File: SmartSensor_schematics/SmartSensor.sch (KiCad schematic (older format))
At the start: 48 parts, among them IC1 DS1337+, J1 Conn_01x01_Female, J2 Conn_01x01_Female, J3 Conn_02x04_Odd_Even, J4 FTDI cable connector, J5 USB_B_Micro, J8 6 PIN ISP, Q1 MMBF170, Q2 2N7002, Q3 2N7002, Q4 2N7002, SW1 SW_Push, U1 LTC3536EMSEPBF, U2 MCP9808_MSOP, U3 DMG2301L, U4 ATmega328-PU, U5 XBee_SMT, X1 XTAL

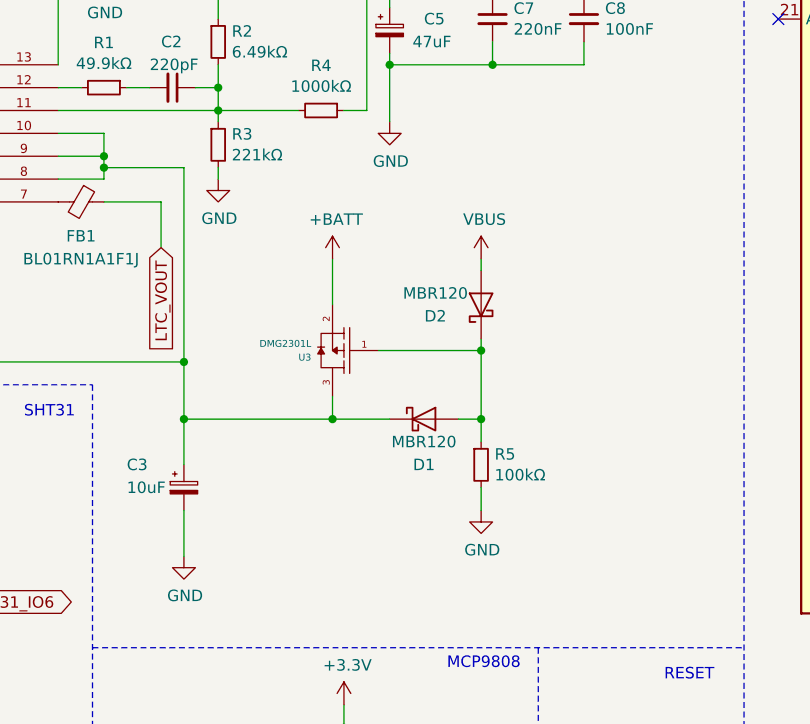
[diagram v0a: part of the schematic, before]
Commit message: delay: increment startup time
Signed-off-by: Michel Megens <dev@bietje.net>
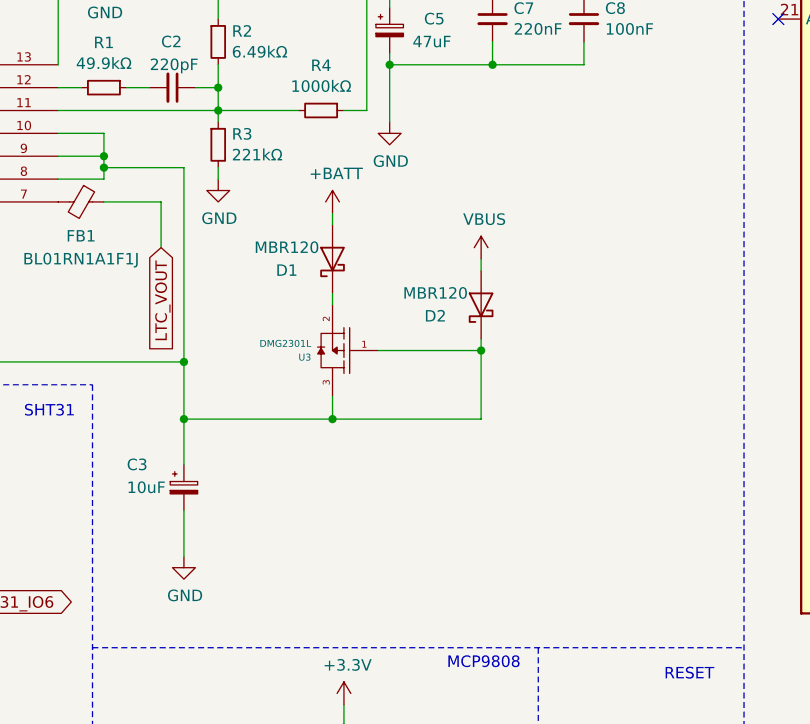
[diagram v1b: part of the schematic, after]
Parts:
- removed R5: 100kΩ, Resistor_SMD:R_1206_3216Metric_Pad1.42x1.75mm_HandSolder, symbol Device:R_Small
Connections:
- net +BATT: now also D1.2 (A); no longer U3.2
- net at C3.1, U1.1 (RT), U1.10 (*SHDN)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: now also D2.1 (K), U3.1; no longer D1.1 (K)
- new net: D1.1 (K), U3.2
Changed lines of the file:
@@
 L power:+BATT #PWR015
 U 1 1 5D0A73DC
-P 4300 2350
-F 0 "#PWR015" H 4300 2200 50  0001 C CNN
-F 1 "+BATT" H 4315 2523 50  0000 C CNN
-F 2 "" H 4300 2350 50  0001 C CNN
-F 3 "" H 4300 2350 50  0001 C CNN
-	1    4300 2350
+P 4300 2150
+F 0 "#PWR015" H 4300 2000 50  0001 C CNN
+F 1 "+BATT" H 4315 2323 50  0000 C CNN
+F 2 "" H 4300 2150 50  0001 C CNN
+F 3 "" H 4300 2150 50  0001 C CNN
+	1    4300 2150
 	1    0    0    -1
 $EndComp
@@
 Text Notes 10600 700  0    50   ~ 0
 Xbee module
-Wire Wire Line
-	4300 2350 4300 2550
 $Comp
 L LTC3536EMSEPBF:LTC3536EMSEPBF U1
@@
 	-1   0    0    1
 $EndComp
-$Comp
-L Device:D_Schottky D1
-U 1 1 5CFE739E
-P 4700 3050
-F 0 "D1" H 4700 2850 50  0000 C CNN
-F 1 "MBR120" H 4700 2950 50  0000 C CNN
-F 2 "Diode_SMD:D_SOD-123F" H 4700 3050 50  0001 C CNN
-F 3 "~" H 4700 3050 50  0001 C CNN
-	1    4700 3050
-	1    0    0    -1
-$EndComp
-Wire Wire Line
-	4950 3050 4850 3050
-Wire Wire Line
-	4300 3050 4550 3050
 Wire Wire Line
 	4950 2750 4950 3050
-$Comp
-L Device:R_Small R5
-U 1 1 5D0B51AA
-P 4950 3250
-F 0 "R5" H 5009 3296 50  0000 L CNN
-F 1 "100kΩ" H 5009 3205 50  0000 L CNN
-F 2 "Resistor_SMD:R_1206_3216Metric_Pad1.42x1.75mm_HandSolder" H 4950 3250 50  0001 C CNN
-F 3 "~" H 4950 3250 50  0001 C CNN
-	1    4950 3250
-	1    0    0    -1
-$EndComp
-Wire Wire Line
-	4950 3050 4950 3150
-$Comp
-L power:GND #PWR021
-U 1 1 5D0C839F
-P 4950 3450
-F 0 "#PWR021" H 4950 3200 50  0001 C CNN
-F 1 "GND" H 4955 3277 50  0000 C CNN
-F 2 "" H 4950 3450 50  0001 C CNN
-F 3 "" H 4950 3450 50  0001 C CNN
-	1    4950 3450
-	1    0    0    -1
-$EndComp
-Wire Wire Line
-	4950 3350 4950 3450
 Connection ~ 4300 3050
 $Comp
@@
 Wire Wire Line
 	8850 5000 8850 5100
-Connection ~ 4950 3050
 Wire Wire Line
 	3300 2100 3550 2100
@@
 Text Notes 10700 3500 0    50   ~ 0
 Connector
+Wire Wire Line
+	4300 3050 4950 3050
+$Comp
+L Device:D_Schottky D1
+U 1 1 5D16F809
+P 4300 2350
+F 0 "D1" V 4250 2550 50  0000 C CNN
+F 1 "MBR120" V 4350 2550 50  0000 C CNN
+F 2 "Diode_SMD:D_SOD-123F" H 4300 2350 50  0001 C CNN
+F 3 "~" H 4300 2350 50  0001 C CNN
+	1    4300 2350
+	0    -1   -1   0
+$EndComp
+Wire Wire Line
+	4300 2150 4300 2200
+Wire Wire Line
+	4300 2500 4300 2550
 $EndSCHEMATC

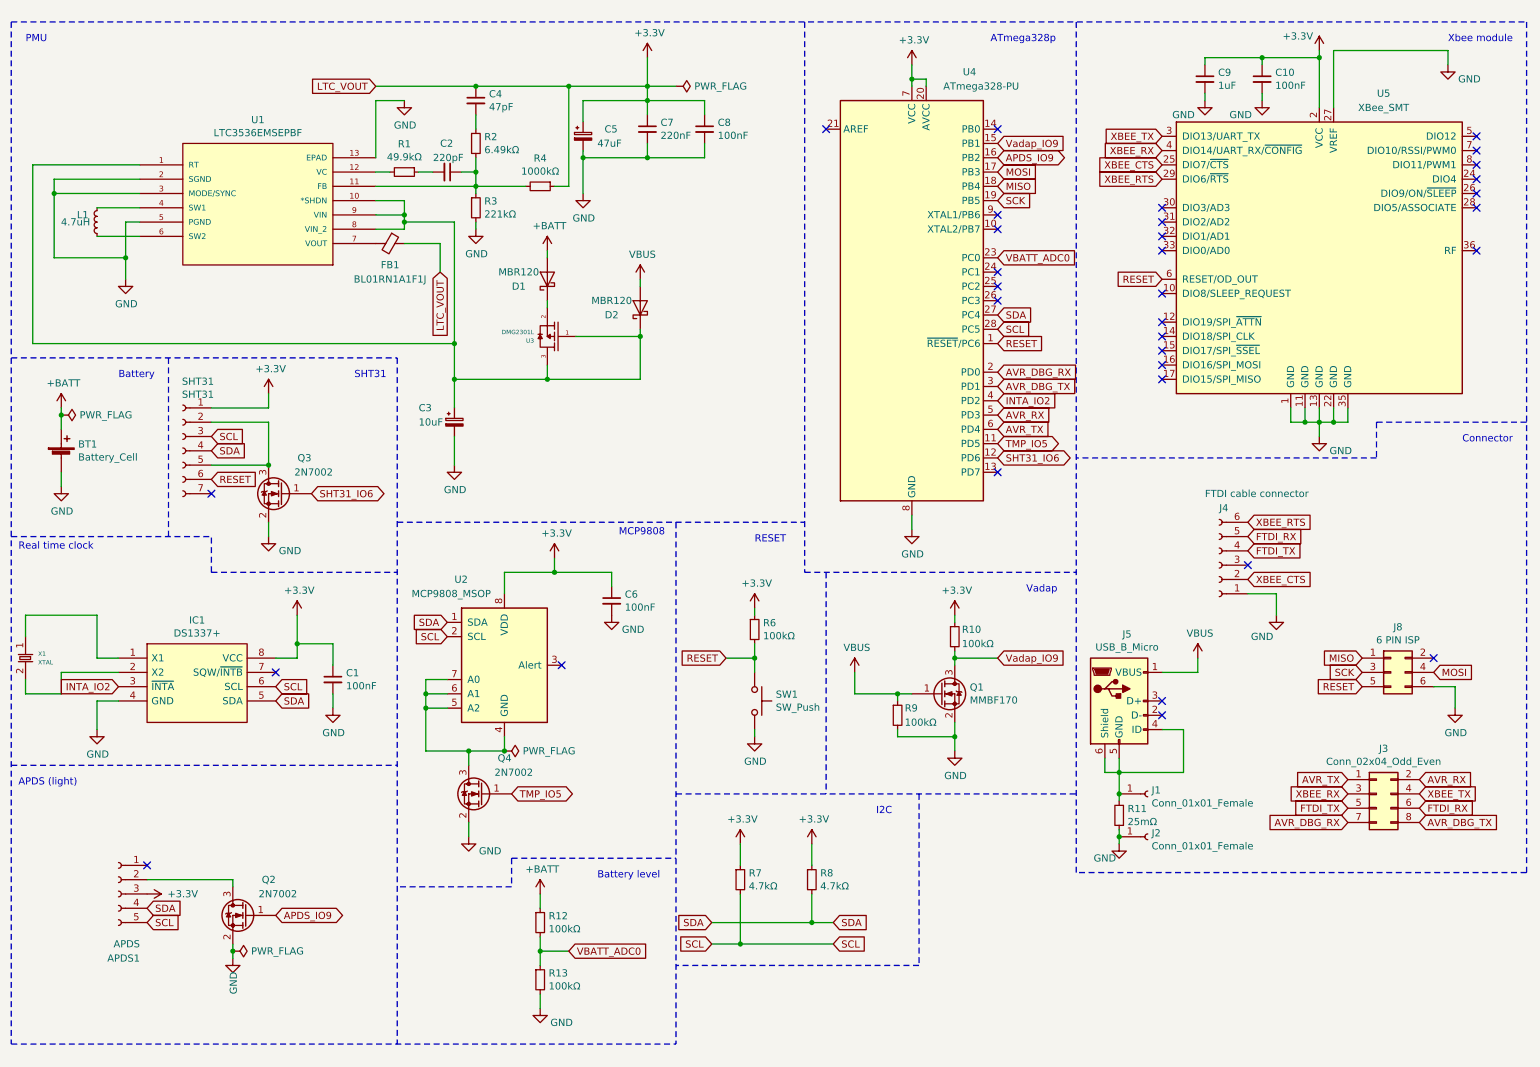
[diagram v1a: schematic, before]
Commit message: schematics: update the schematics to v3
Update schematics to version 3.

Signed-off-by: Michel Megens <michel@michelmegens.net>
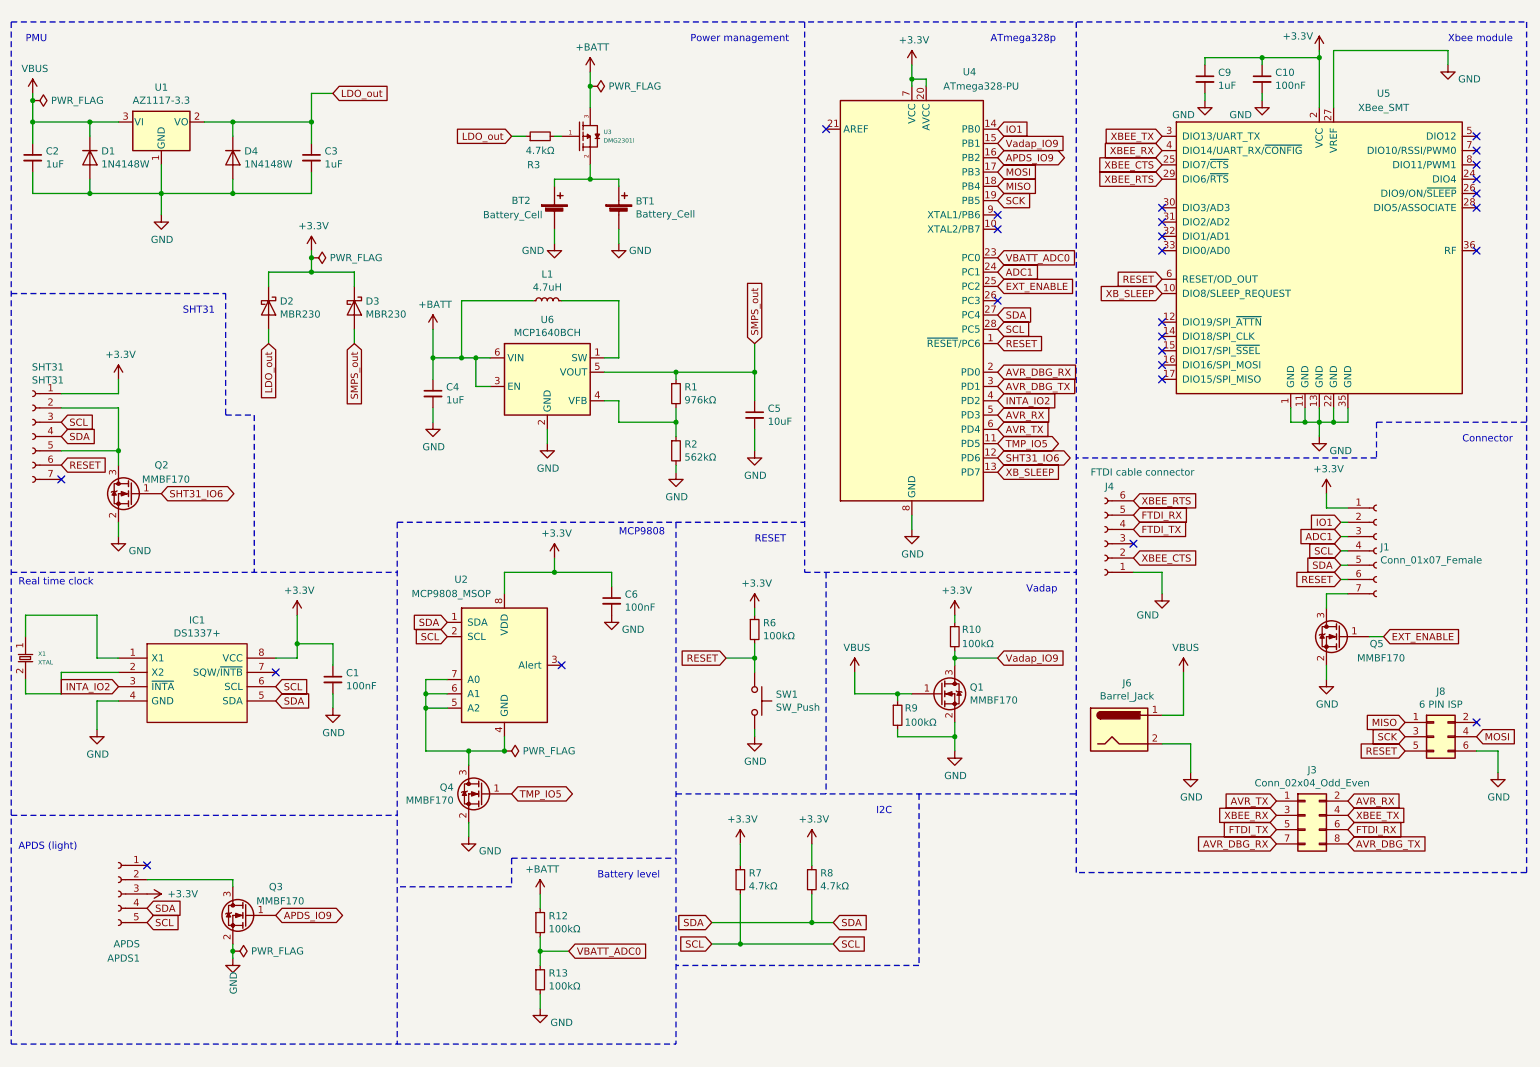
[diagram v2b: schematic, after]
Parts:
- removed C3: 10uF, Capacitor_THT:CP_Radial_D5.0mm_P2.00mm, symbol Device:CP_Small
- removed C5: 47uF, Capacitor_THT:CP_Radial_D5.0mm_P2.00mm, symbol Device:CP_Small
- removed C7: 220nF, Capacitor_SMD:C_1206_3216Metric_Pad1.42x1.75mm_HandSolder, symbol Device:C_Small
- removed C8: 100nF, Capacitor_SMD:C_1206_3216Metric_Pad1.42x1.75mm_HandSolder, symbol Device:C_Small
- removed D1: MBR120, Diode_SMD:D_SOD-123F, symbol Device:D_Schottky
- removed FB1: BL01RN1A1F1J, Inductor_THT:L_Axial_L5.3mm_D2.2mm_P10.16mm_Horizontal_Vishay_IM-1, symbol Device:Ferrite_Bead_Small
- removed J1, J2: Conn_01x01_Female, Connector_PinHeader_2.54mm:PinHeader_1x01_P2.54mm_Vertical, symbol Connector:Conn_01x01_Female
- removed J5: USB_B_Micro, Connector_USB:USB_Micro-B_Molex_47346-0001, symbol Connector:USB_B_Micro
- removed Q2, Q3, Q4: 2N7002, Package_TO_SOT_SMD:SOT-23, symbol Transistor_FET:2N7002
- removed R11: 25mΩ, Resistor_SMD:R_1206_3216Metric_Pad1.42x1.75mm_HandSolder, symbol Device:R_Small
- removed R4: 1000kΩ, Resistor_SMD:R_1206_3216Metric_Pad1.42x1.75mm_HandSolder, symbol Device:R_Small
- removed U1: LTC3536EMSEPBF, LTC3536EMSEPBF:MSOP-12_MSE, symbol LTC3536EMSEPBF:LTC3536EMSEPBF
- added BT2: Battery_Cell, BatteryPack:2460, symbol Device:Battery_Cell
- added C3: 1uF, Capacitor_SMD:C_1206_3216Metric_Pad1.42x1.75mm_HandSolder, symbol Device:C_Small
- added C5: 10uF, Capacitor_SMD:C_1206_3216Metric_Pad1.42x1.75mm_HandSolder, symbol Device:C_Small
- added D1, D4: 1N4148W, Diode_SMD:D_SOD-123, symbol Diode:1N4148W
- added D3: MBR230, Diode_SMD:D_SOD-123F, symbol Device:D_Schottky
- added J1: Conn_01x07_Female, Connector_PinSocket_2.54mm:PinSocket_1x07_P2.54mm_Vertical, symbol Connector:Conn_01x07_Female
- added J6: Barrel_Jack, Connector_BarrelJack:BarrelJack_Wuerth_6941xx301002, symbol Connector:Barrel_Jack
- added Q2, Q3, Q4, Q5: MMBF170, Package_TO_SOT_SMD:SOT-23, symbol Transistor_FET:MMBF170
- added U1: AZ1117-3.3, Package_TO_SOT_SMD:SOT-223-3_TabPin2, symbol Regulator_Linear:AZ1117-3.3
- added U6: MCP1640BCH, Package_TO_SOT_SMD:SOT-23-6, symbol Regulator_Switching:MCP1640BCH
- BT1: footprint Battery:BatteryHolder_Keystone_2462_2xAA -> BatteryPack:2460
- C2: value 220pF -> 1uF
- C4: value 47pF -> 1uF
- D2: value MBR120 -> MBR230
- L1: footprint Inductor_SMD:L_1210_3225Metric_Pad1.42x2.65mm_HandSolder -> Inductor_SMD:L_Coilcraft_XxL4040
- R1: value 49.9kΩ -> 976kΩ
- R2: value 6.49kΩ -> 562kΩ
- R3: value 221kΩ -> 4.7kΩ
- U3: value DMG2301L -> DMG2301l
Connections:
- net +3V3: now also D2.1 (K), D3.1 (K), J1.1 (Pin_1); no longer C4.1
- net +BATT: now also C4.1, L1.1, U3.3, U6.3 (EN), U6.6 (VIN); no longer BT1.1 (+)
- net APDS_IO9: now also Q3.1 (G)
- net GND: now also C2.2, C4.2, R2.2, BT2.2 (-), C3.2, C5.2, D1.2 (A), D4.2 (A), J6.2, Q2.2 (S), Q3.2 (S), Q4.2 (S), Q5.2 (S), U1.1 (GND), U6.2 (GND); no longer R3.2
- net RESET: now also J1.6 (Pin_6)
- net SCL: now also J1.4 (Pin_4)
- net SDA: now also J1.5 (Pin_5)
- net SHT31_IO6: now also Q2.1 (G)
- net TMP_IO5: now also Q4.1 (G)
- net VBUS: now also C2.1, D1.1 (K), J6.1, U1.3 (VI); no longer D2.2 (A)
- net at U2.4 (GND), U2.5 (A2), U2.6 (A1)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: now also Q4.3 (D)
- net at R1.2: now also R2.1, U6.4 (VFB)
- net at L1.2: now also U6.1 (SW)
- net XB_SLEEP: now reaches U5.10 (DIO8/SLEEP_REQUEST)
- net XB_SLEEP: now also U4.13 (PD7)
- net IO1: now reaches U4.14 (PB0)
- net IO1: now also J1.2 (Pin_2)
- net ADC1: now reaches U4.24 (PC1)
- net ADC1: now also J1.3 (Pin_3)
- net EXT_ENABLE: now reaches U4.25 (PC2)
- net EXT_ENABLE: now also Q5.1 (G)
- net at U3.2: now also BT1.1 (+), BT2.1 (+)
- net SMPS_out: now reaches R1.1
- net SMPS_out: now also C5.1, D3.2 (A), U6.5 (VOUT); no longer C2.2
- net at SHT31.2 (Pin_2), SHT31.5 (Pin_5): now also Q2.3 (D)
- net at APDS1.2 (Pin_2): now also Q3.3 (D)
- new net: J1.7 (Pin_7), Q5.3 (D)
- new net: R3.2, U3.1
- new net LDO_out: C3.1, D2.2 (A), D4.1 (K), R3.1, U1.2 (VO)
- no-connect marks 33 -> 26
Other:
- note added: "Power management"
- note removed: "Battery"
- moved on the sheet: J3, J4, J8, SHT31

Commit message: schematics: implement version 3
Implement the version 3 schematics.

Signed-off-by: Michel Megens <michel@michelmegens.net>
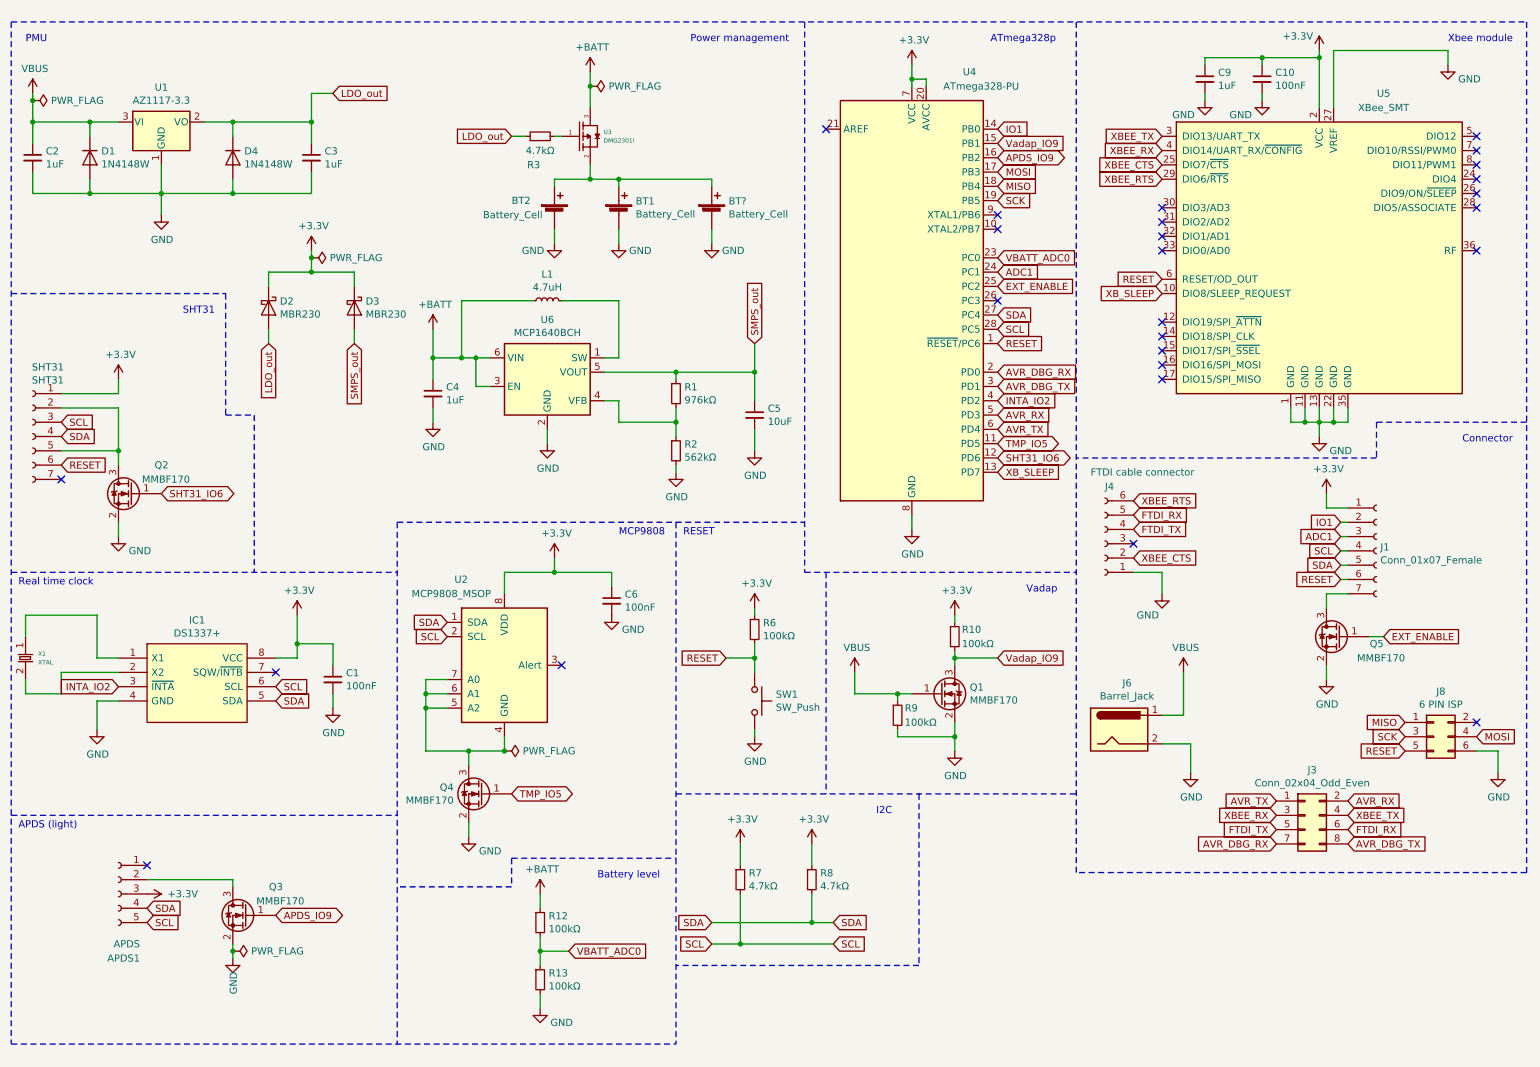
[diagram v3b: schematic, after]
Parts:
- added BT?: Battery_Cell, BatteryPack:2460, symbol Device:Battery_Cell
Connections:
- net GND: now also BT?.2 (-)
- net at BT1.1 (+), BT2.1 (+), U3.2: now also BT?.1 (+)
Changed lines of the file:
@@
 Wire Notes Line
 	550  550  11150 550
-Text Notes 5750 4200 0    50   ~ 0
+Text Notes 5250 4150 0    50   ~ 0
 RESET
 Wire Notes Line
@@
 Text Notes 650  700  0    50   ~ 0
 PMU
-Text Notes 600  6350 0    50   ~ 0
+Text Notes 600  6200 0    50   ~ 0
 APDS (light)
 Text Notes 7650 4550 0    50   ~ 0
@@
 Wire Wire Line
 	4350 2000 4350 2100
+$Comp
+L Device:Battery_Cell BT?
+U 1 1 5DD19F34
+P 5450 1900
+F 0 "BT?" H 5568 1996 50  0000 L CNN
+F 1 "Battery_Cell" H 5568 1905 50  0000 L CNN
+F 2 "BatteryPack:2460" V 5450 1960 50  0001 C CNN
+F 3 "~" V 5450 1960 50  0001 C CNN
+	1    5450 1900
+	1    0    0    -1
+$EndComp
+$Comp
+L power:GND #PWR?
+U 1 1 5DD19FC8
+P 5450 2100
+F 0 "#PWR?" H 5450 1850 50  0001 C CNN
+F 1 "GND" H 5600 2050 50  0000 C CNN
+F 2 "" H 5450 2100 50  0001 C CNN
+F 3 "" H 5450 2100 50  0001 C CNN
+	1    5450 2100
+	1    0    0    -1
+$EndComp
+Wire Wire Line
+	5450 2000 5450 2100
+Wire Wire Line
+	4800 1650 5450 1650
+Wire Wire Line
+	5450 1650 5450 1700
+Connection ~ 4800 1650
 $EndSCHEMATC
